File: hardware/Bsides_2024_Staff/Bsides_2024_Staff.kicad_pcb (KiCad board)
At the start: 2 copper layers, 98.5 x 98.3 mm, 33 parts, among them J1 UART, J3 OLED, J4 I2C, Q1 DMG3415U-7, SW2 RESET, SW3 GPIO, SW4 RESET, SW5 RESET, SW6 RESET, SW7 RESET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

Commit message: feat(Hw):Init_Floorplan
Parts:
- added SW1: ON, bsides:MSK12C02, F.Cu at (227.8, 60.9)
- SW3: value GPIO -> BOOT
- SW5, SW7: value RESET -> ~
- moved U1 172.2 mm to (149.6, 114.1), turned to 180 degrees
- moved SW7 70.7 mm to (125.0, 74.6)
- moved J3 69.9 mm to (131.4, 71.1)
- moved SW2 62.7 mm to (131.5, 51.0)
- moved SW6 52.0 mm to (143.4, 93.5)
- moved SW4 46.4 mm to (167.0, 105.5)
- moved SW5 42.0 mm to (156.3, 93.3)
- moved C1 29.5 mm to (185.1, 76.4), turned to 90 degrees
- moved SW3 27.4 mm to (167.8, 53.1)
- moved C2 24.3 mm to (190.9, 76.1), turned to -90 degrees
- moved U2 22.1 mm to (188.0, 76.2)

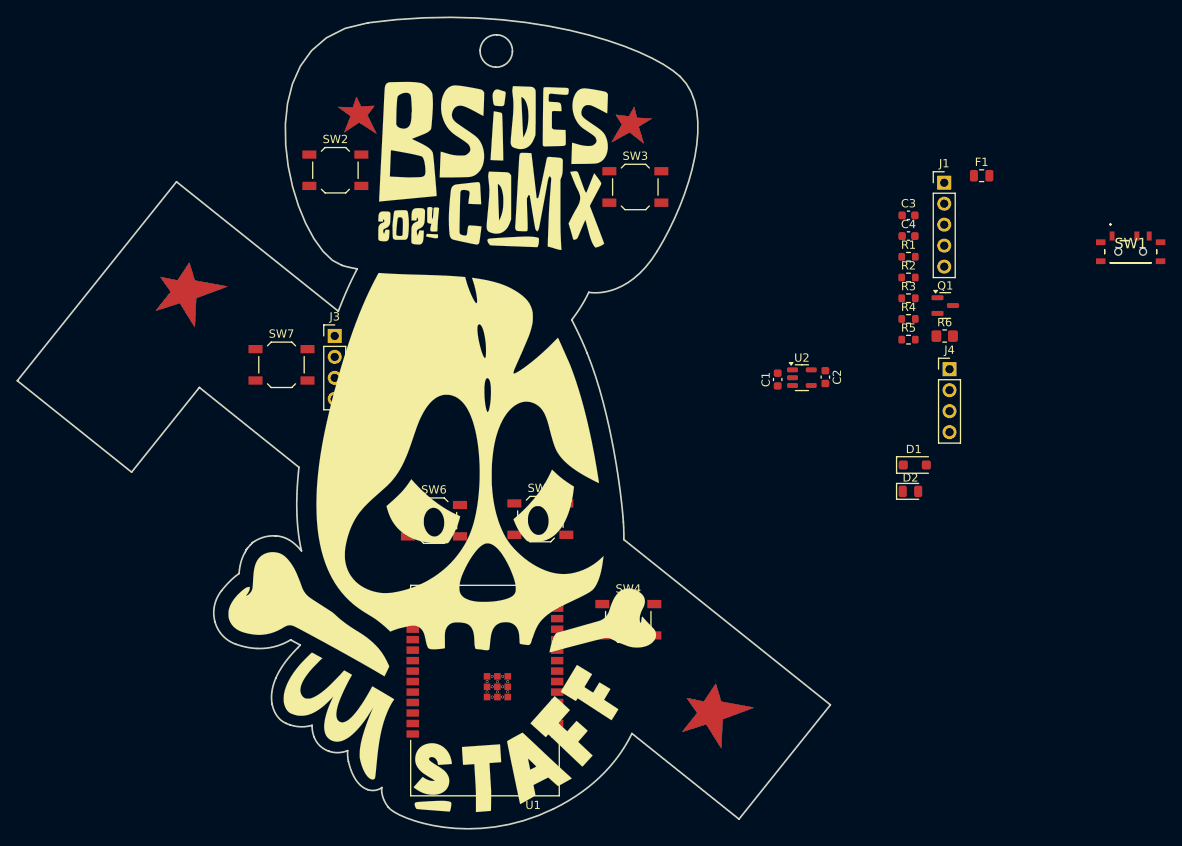
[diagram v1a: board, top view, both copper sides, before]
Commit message: feat(Hw):Add_Preview
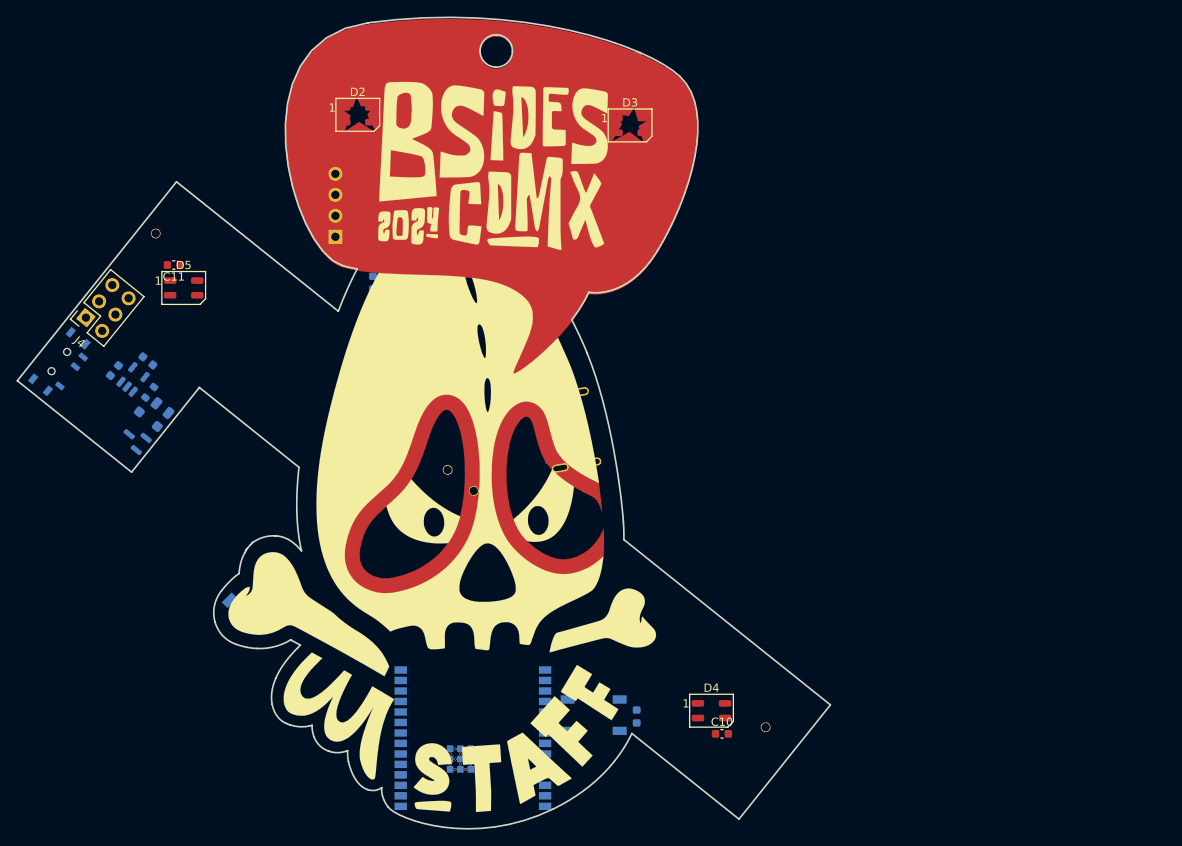
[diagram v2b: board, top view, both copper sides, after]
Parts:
- removed R6: 330R, Resistor_SMD:R_0805_2012Metric_Pad1.20x1.40mm_HandSolder
- removed the Ref** at (189.1, 147.4) (x2)
- removed the Ref** at (150.4, 75.5)
- removed the Ref** at (142.8, 82.6)
- added C10: 0.1uF, Capacitor_SMD:C_0603_1608Metric, F.Cu at (178.3, 119.3)
- added C11: 0.1uF, Capacitor_SMD:C_0603_1608Metric, F.Cu at (111.9, 62.5)
- added C12: 0.1uF, Capacitor_SMD:C_0603_1608Metric, B.Cu at (128.2, 48.4)
- added C5: 0.1uF, Capacitor_SMD:C_0603_1608Metric, B.Cu at (157.9, 69.7)
- added C6: 0.1uF, Capacitor_SMD:C_0603_1608Metric, B.Cu at (168.0, 117.2)
- added C7: 0.1uF, Capacitor_SMD:C_0603_1608Metric, B.Cu at (125.0, 105.0)
- added C8: 0.1uF, Capacitor_SMD:C_0603_1608Metric, B.Cu at (136.1, 64.7)
- added C9: 0.1uF, Capacitor_SMD:C_0603_1608Metric, B.Cu at (164.4, 48.4)
- added D3: WS2812B, LED_SMD:LED_WS2812B-Mini_PLCC4_3.5x3.5mm, F.Cu at (167.2, 45.6)
- added D4: WS2812B, LED_SMD:LED_WS2812B-Mini_PLCC4_3.5x3.5mm, F.Cu at (177.1, 116.5)
- added D5: WS2812B, LED_SMD:LED_WS2812B-Mini_PLCC4_3.5x3.5mm, F.Cu at (113.1, 65.3)
- added J2: Battery, bsides:BH-AAA-A1aj001, B.Cu at (127.4, 73.0)
- added P1: USB_C_Plug_USB2.0, bsides:C393939, B.Cu at (158.0, 82.8)
- added R7: 470, Resistor_SMD:R_0603_1608Metric, B.Cu at (168.4, 48.3)
- C1, C2, D1, F1, Q1, R1, R2, R3, R4, R5, SW1, SW2, SW3, SW4, SW5, SW6, SW7, U1, U2: moved to B.Cu
- C3, C4: value .1uF -> 0.1uF; moved to B.Cu
- D2: value RED -> WS2812B; footprint LED_SMD:LED_0805_2012Metric -> LED_SMD:LED_WS2812B-Mini_PLCC4_3.5x3.5mm
- J1: value UART -> Battery; footprint Connector_PinHeader_2.54mm:PinHeader_1x05_P2.54mm_Vertical -> bsides:BH-AAA-A1aj001; moved to B.Cu
- J3: footprint Connector_PinHeader_2.54mm:PinHeader_1x04_P2.54mm_Vertical -> bsides:Display OLED 128 x32; moved to B.Cu
- J4: value I2C -> Conn_02x03_Odd_Even; footprint Connector_PinHeader_2.54mm:PinHeader_1x04_P2.54mm_Vertical -> Connector_PinSocket_2.54mm:PinSocket_2x03_P2.54mm_Vertical
- moved SW1 130.5 mm to (98.1, 74.2), turned to 51 degrees
- moved J4 104.8 mm to (101.3, 68.9), turned to 141 degrees
- moved F1 103.1 mm to (110.6, 79.8), turned to 141 degrees
- moved Q1 99.4 mm to (107.3, 83.6), turned to 141 degrees
- moved D1 93.0 mm to (108.8, 81.2), turned to -39 degrees
- moved R2 93.0 mm to (109.0, 77.9), turned to 51 degrees
- moved C2 86.1 mm to (104.8, 75.3), turned to 51 degrees
- moved U2 81.0 mm to (107.0, 76.4), turned to 51 degrees
- moved D2 81.0 mm to (134.2, 44.3)
- moved C1 76.3 mm to (108.8, 74.1), turned to 141 degrees
- moved R5 73.5 mm to (133.9, 41.4), turned to 180 degrees
- moved J1 64.9 mm to (166.0, 104.2), turned to -39 degrees
- moved C4 64.2 mm to (139.2, 41.5)
- moved R1 48.8 mm to (152.8, 69.7), turned to 180 degrees
- moved R3 48.7 mm to (158.2, 89.9), turned to -170 degrees
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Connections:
- net /LED1 renamed /PIN
- D2 pad 1: GND -> +3V3
- D2 pad 2: Net-(D2-A) -> unconnected-(D2-DOUT-Pad2)
- J1 pad 1: +3V3 -> GND
- J1 pad 2: /RX -> Net-(J1-Pin_2)
- J4 pad 1: +3V3 -> unconnected-(J4-Pin_1-Pad1)
- J4 pad 2: /SCL -> unconnected-(J4-Pin_2-Pad2)
- J4 pad 3: /SDA -> unconnected-(J4-Pin_3-Pad3)
- J4 pad 4: GND -> unconnected-(J4-Pin_4-Pad4)

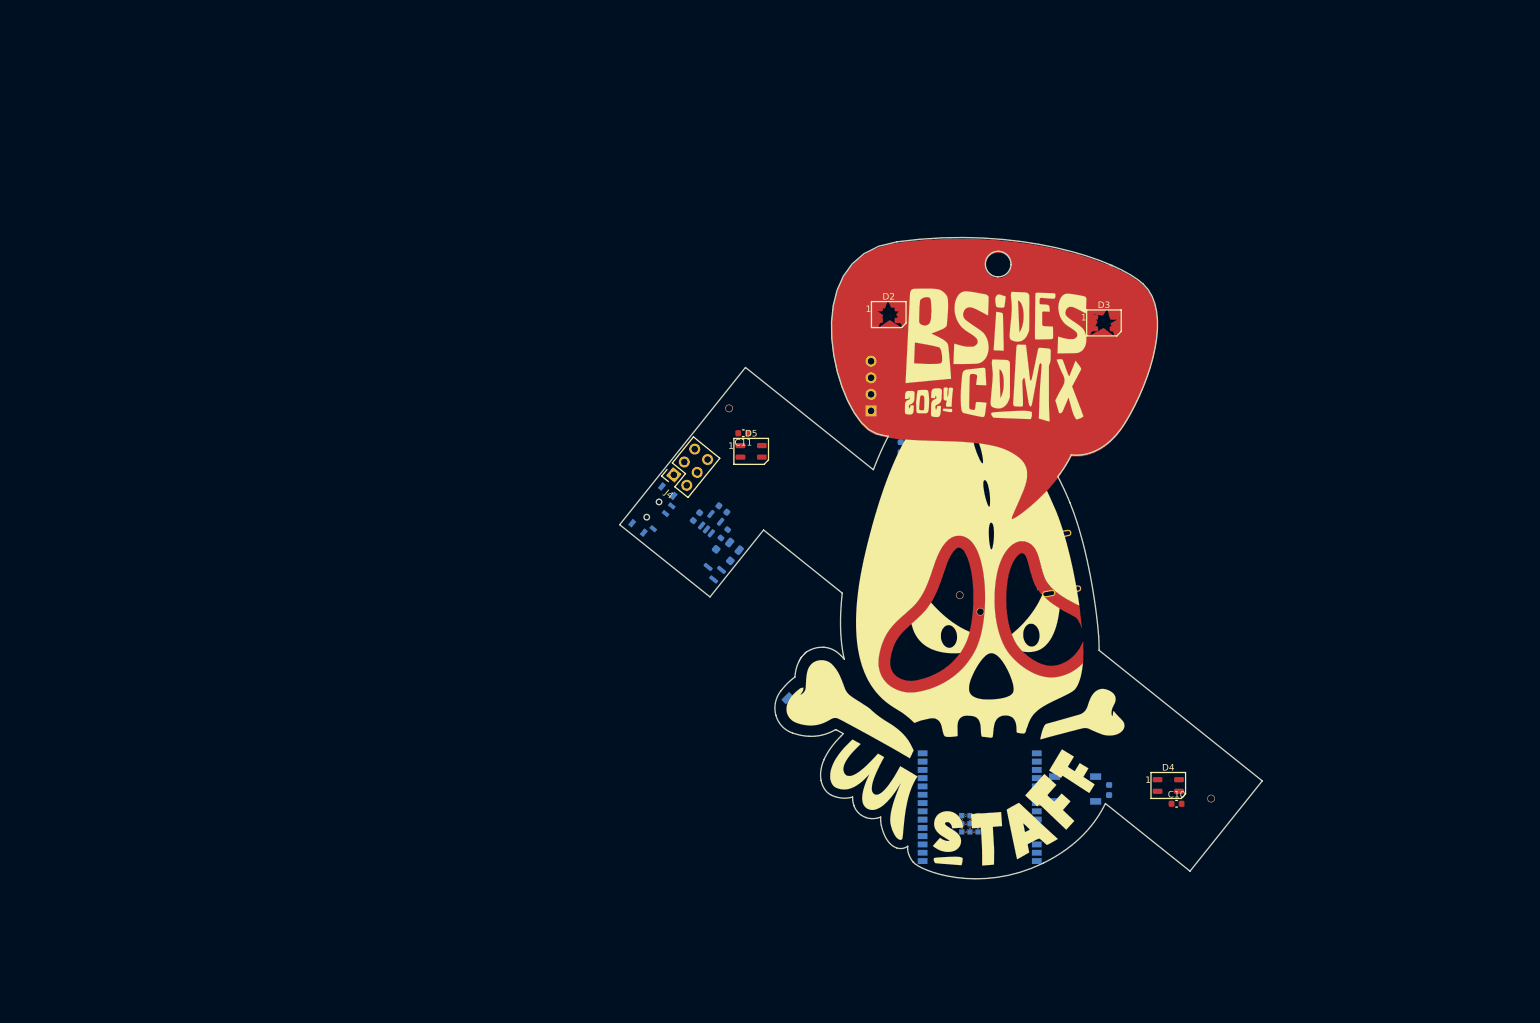
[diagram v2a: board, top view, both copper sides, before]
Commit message: feat(Hw):Added_speaker_Badge_Floorplan
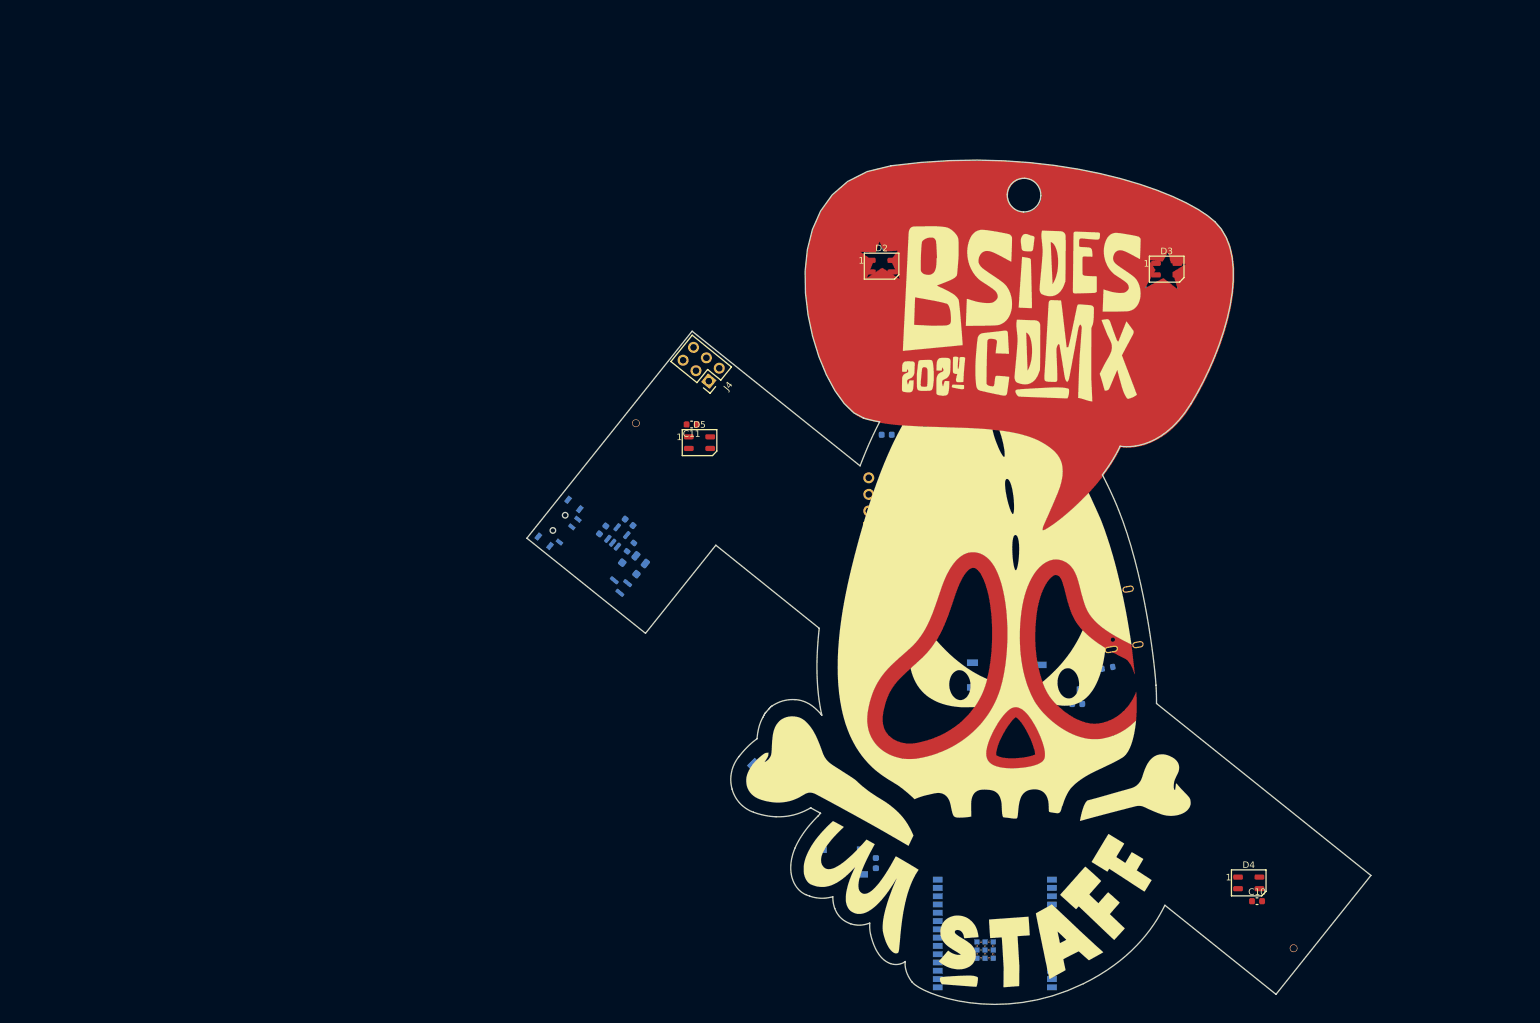
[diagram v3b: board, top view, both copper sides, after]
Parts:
- removed the Ref** at (146.0, 81.6) (x2)
- removed the Ref** at (150.4, 75.5)
- removed the Ref** at (142.8, 82.6)
- added Ref**: Val**, Staff:Badge Staff_Bsides 2024 CDMX (1), F.Cu at (148.4, 84.0)
- moved C6 37.5 mm to (132.2, 128.4)
- moved SW5 37.5 mm to (127.0, 128.2)
- moved C5 34.8 mm to (163.1, 104.0)
- moved R1 34.8 mm to (158.1, 104.0)
- moved SW4 34.8 mm to (160.7, 99.9)
- moved C8 33.5 mm to (138.9, 98.1)
- moved SW7 33.5 mm to (143.9, 99.6)
- moved J1 26.2 mm to (178.6, 127.1)
- moved U1 19.5 mm to (150.5, 142.2)
- moved C10 19.4 mm to (190.7, 134.2)
- moved D4 19.4 mm to (189.4, 131.4)
- moved J3 17.9 mm to (131.2, 77.0)
- moved C12 15.4 mm to (133.9, 62.7)
- moved J4 15.3 mm to (106.6, 54.5), turned to -129 degrees
- moved C1 14.5 mm to (94.4, 76.2)
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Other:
- board size 98.5 x 98.3 mm -> 129.4 x 129.4 mm

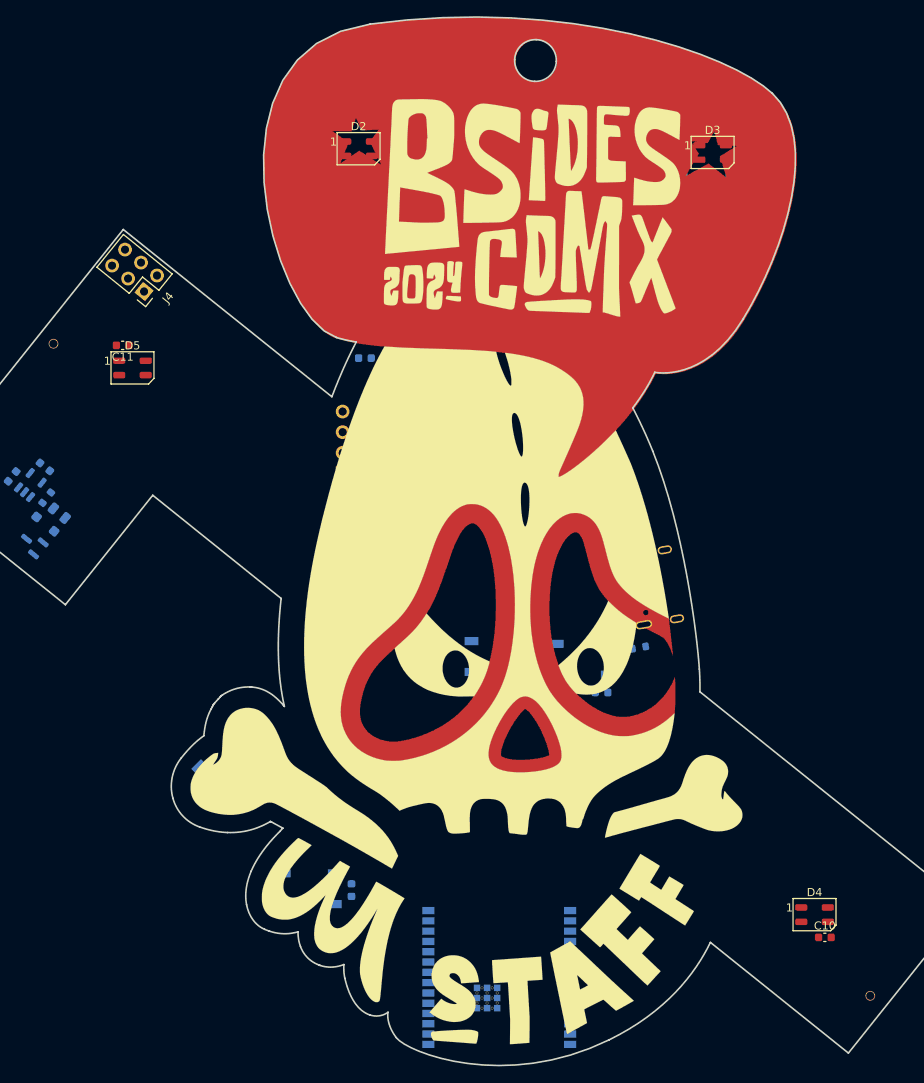
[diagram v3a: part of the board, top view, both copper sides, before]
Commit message: feat(Hw):Update_Route_Speaker
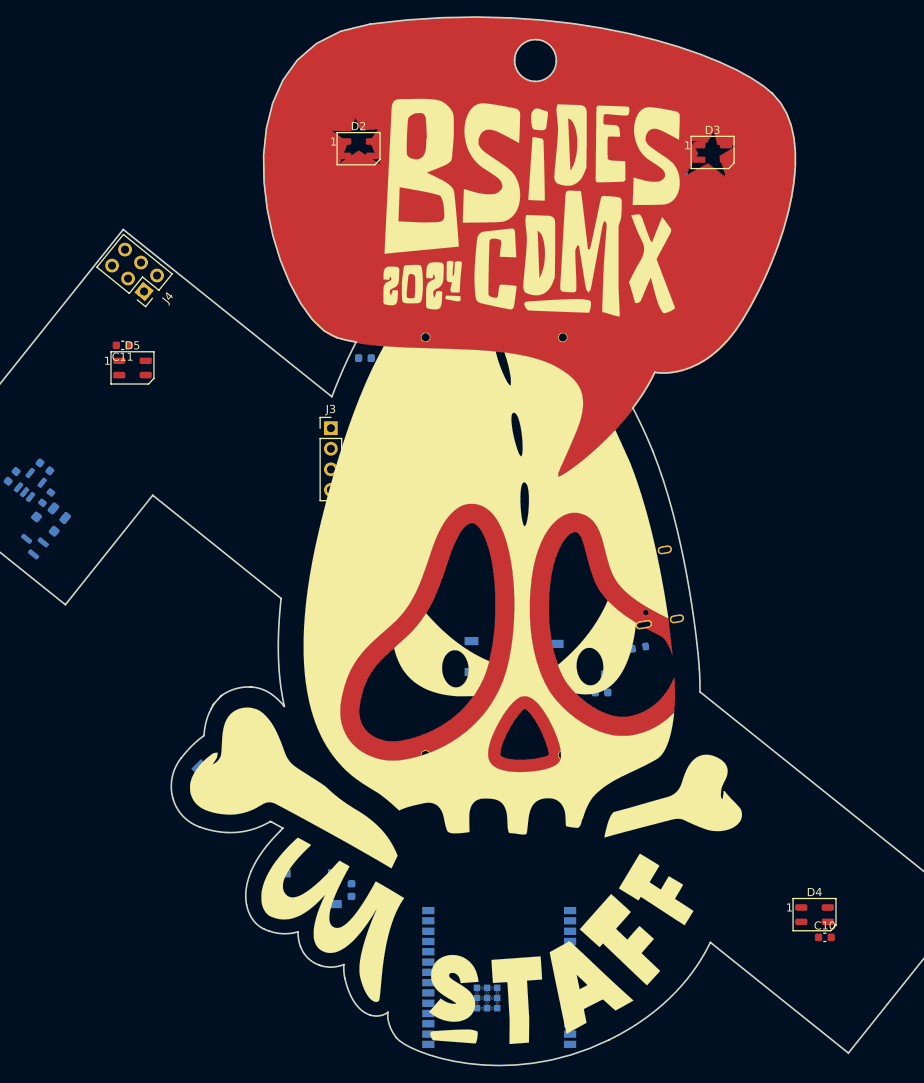
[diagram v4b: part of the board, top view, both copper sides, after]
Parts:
- J1, J2: footprint bsides:BH-AAA-A1aj001 -> bsides:BH-AA-A1AJ020
- J3: moved to F.Cu
- moved J1 55.5 mm to (141.4, 86.0), turned to 90 degrees
- moved J2 46.4 mm to (158.3, 86.0), turned to -90 degrees
- moved J3 5.76 mm to (129.7, 71.4)
- moved Ref** 0.07 mm to (148.4, 84.0)

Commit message: feat:(Hw)Update_PCB_Speaker_Sponsor_Staff
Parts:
- removed the Ref** at (148.4, 84.0)
- added C13: 1uF, Capacitor_SMD:C_0603_1608Metric, B.Cu at (138.5, 140.6)
- added C14: 10uF, Capacitor_SMD:C_0603_1608Metric, B.Cu at (138.5, 142.1)
- added C15: 10uF, Capacitor_SMD:C_0603_1608Metric, B.Cu at (138.5, 143.6)
- added Ref**: Val**, Staff:Badge_Staff_Bsides_2024_CDMX, F.Cu at (145.8, 83.8)
- J4: value Conn_02x03_Odd_Even -> Add_On
- moved SW3 101.3 mm to (170.9, 132.1)
- moved C3 101.3 mm to (173.7, 135.9)
- moved SW1 100.5 mm to (178.5, 109.6), turned to -39 degrees
- moved C4 99.8 mm to (127.3, 133.2)
- moved SW2 99.4 mm to (129.2, 129.5)
- moved R5 99.3 mm to (130.4, 133.3), turned to 0 degrees
- moved C2 91.3 mm to (174.0, 113.9), turned to -129 degrees
- moved U2 85.5 mm to (171.0, 112.6), turned to -129 degrees
- moved C1 84.2 mm to (169.0, 115.2), turned to -39 degrees
- moved R2 80.7 mm to (169.3, 110.8), turned to -129 degrees
- moved Q1 80.5 mm to (171.0, 105.1), turned to -39 degrees
- moved D1 78.8 mm to (169.4, 107.5), turned to 141 degrees
- moved F1 67.9 mm to (163.3, 92.5), turned to -80 degrees
- moved C6 58.2 mm to (190.1, 122.1)
- moved SW5 58.2 mm to (184.9, 121.9)
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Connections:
- C1 pad 1: Net-(SW1-B) -> VBUS
- C10 pad 2: +3V3 -> /VOUT
- C11 pad 2: +3V3 -> /VOUT
- C12 pad 2: +3V3 -> /VOUT
- C2 pad 1: +3V3 -> Net-(D1-A)
- C9 pad 2: +3V3 -> /VOUT
- D1 pad 2: VBUS -> Net-(D1-A)
- D2 pad 1: +3V3 -> /VOUT
- D3 pad 1: +3V3 -> /VOUT
- D4 pad 1: +3V3 -> /VOUT
- D5 pad 1: +3V3 -> /VOUT
- J3 pad 1: +3V3 -> /VOUT
- J4 pad 1: unconnected-(J4-Pin_1-Pad1) -> /VOUT
- J4 pad 2: unconnected-(J4-Pin_2-Pad2) -> GND
- J4 pad 3: unconnected-(J4-Pin_3-Pad3) -> /SDA
- J4 pad 4: unconnected-(J4-Pin_4-Pad4) -> /SCL
- Q1 pad 1: VBUS -> Net-(D1-A)
- R1 pad 2: +3V3 -> /VOUT
- R2 pad 1: VBUS -> Net-(D1-A)
- R5 pad 2: +3V3 -> /VOUT
- SW1 pad 2: Net-(SW1-B) -> /VOUT
- U1 pad 2: +3V3 -> /VOUT
- U2 pad 1: Net-(SW1-B) -> VBUS
- U2 pad 3: Net-(SW1-B) -> VBUS
- U2 pad 5: +3V3 -> Net-(D1-A)
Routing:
- net VBUS: track 0.00 -> 35.3 mm, vias 0 -> 2
- net +BATT: track 0.00 -> 31.9 mm
- net /VOUT: track 0.00 -> 23.6 mm
- net /EN: track 0.00 -> 21.8 mm
- net Net-(D1-K): track 0.00 -> 20.6 mm
- net Net-(D1-A): track 0.00 -> 16.3 mm
- net GND: track 0.00 -> 13.0 mm
- net Net-(F1-Pad1): track 0.00 -> 12.2 mm
- net /GPIO23: track 0.00 -> 8.33 mm
- net Net-(P1-CC): track 0.00 -> 3.93 mm
- net /PIN: track 0.00 -> 3.70 mm
- net Net-(P1-VCONN): track 0.00 -> 3.39 mm
- added copper zone on F.Cu, net GND
